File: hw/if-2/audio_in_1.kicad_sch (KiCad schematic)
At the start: 33 parts, among them U61 TL072, U62 TL072

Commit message: Documentation improvements, moved a OVP circuit
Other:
- title: COS/CTCSS/PTT Controls (Radio 1) -> Audio Input (Radio 1)
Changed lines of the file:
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@@
 	(paper "USLetter")
 	(title_block
-		(title "COS/CTCSS/PTT Controls (Radio 1)")
-		(date "2025-05-13")
+		(title "Audio Input (Radio 1)")
+		(date "2025-05-31")
 		(rev "2")
 		(company "Bruce MacKinnon KC1FSZ")

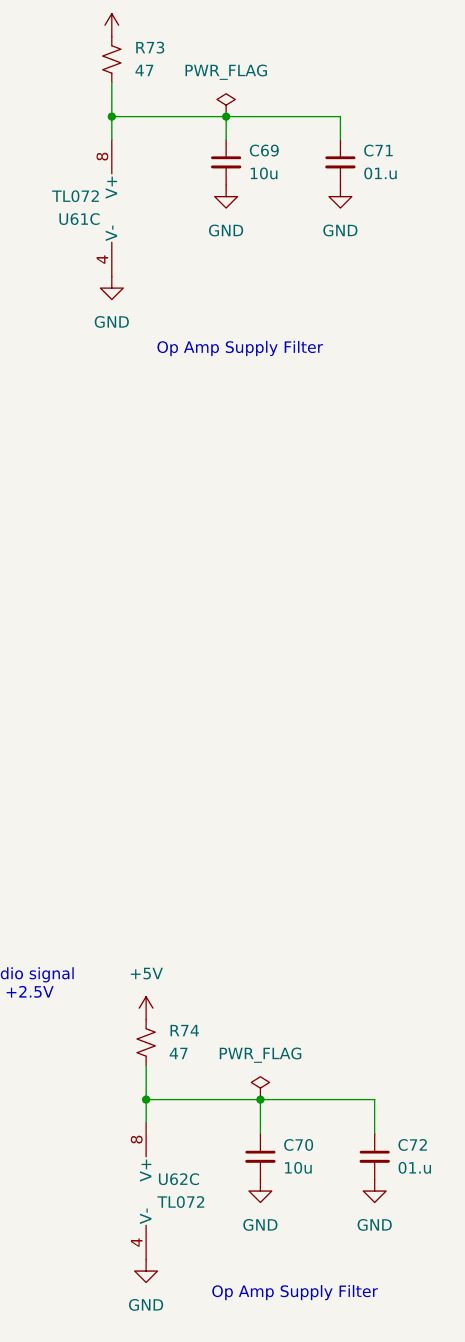
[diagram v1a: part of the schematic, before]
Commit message: Added audio clip
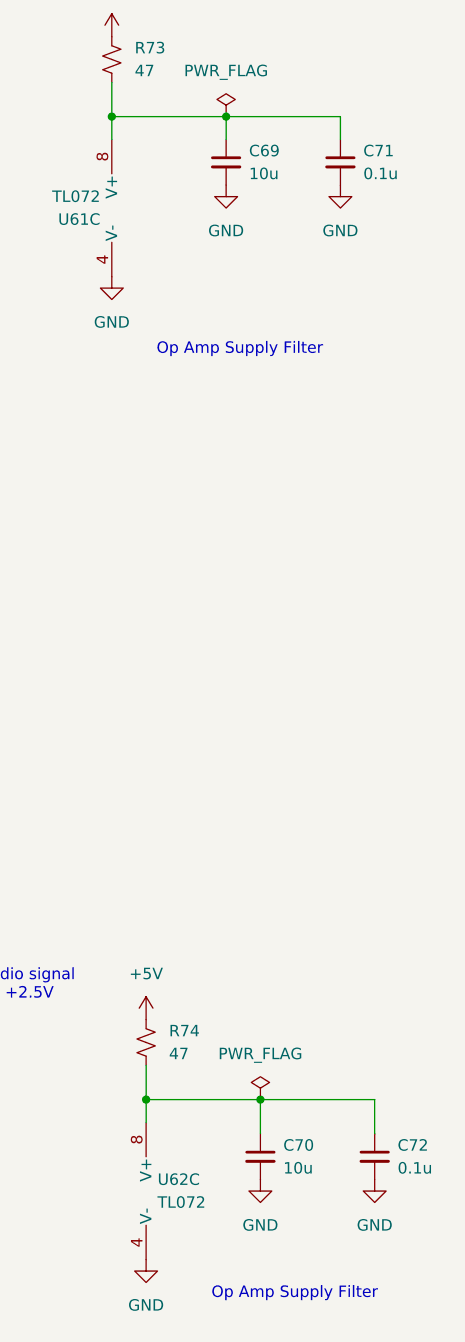
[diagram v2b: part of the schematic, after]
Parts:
- C71, C72: value 01.u -> 0.1u
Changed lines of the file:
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@@
 			)
 		)
-		(property "Value" "01.u"
+		(property "Value" "0.1u"
 			(at 248.92 36.8362 0)
 			(effects
@@
 			)
 		)
-		(property "Value" "01.u"
+		(property "Value" "0.1u"
 			(at 252.73 147.3262 0)
 			(effects

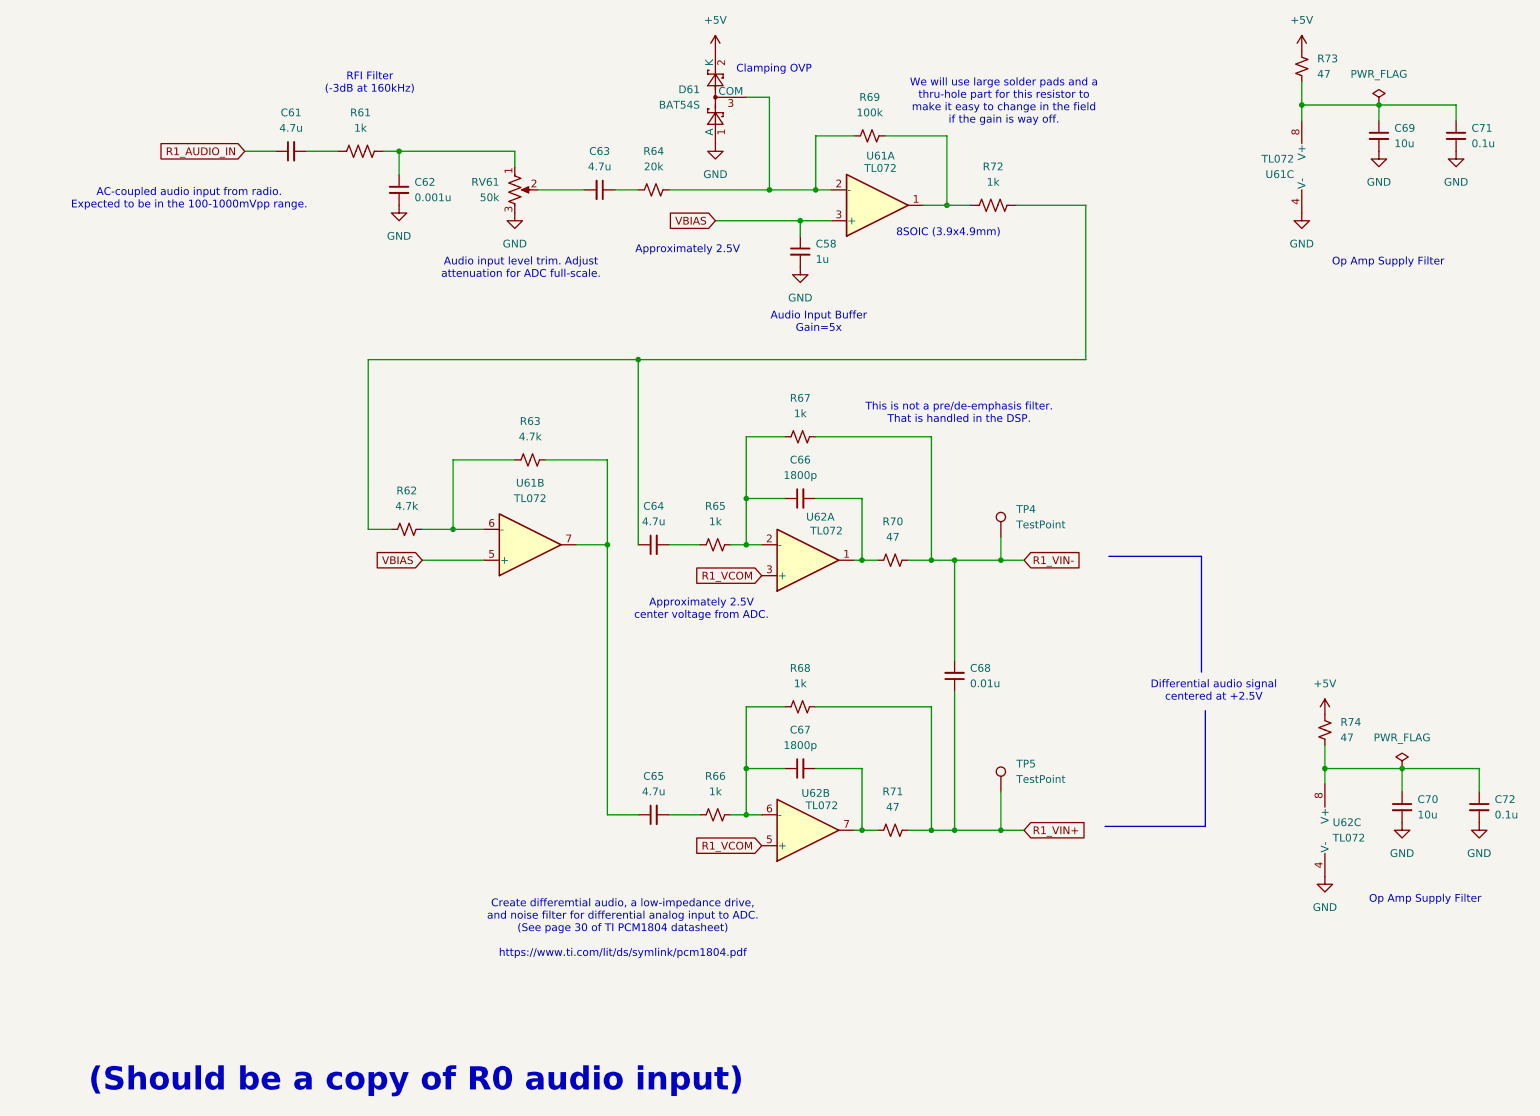
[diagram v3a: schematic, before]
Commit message: Updated audio file to 16K
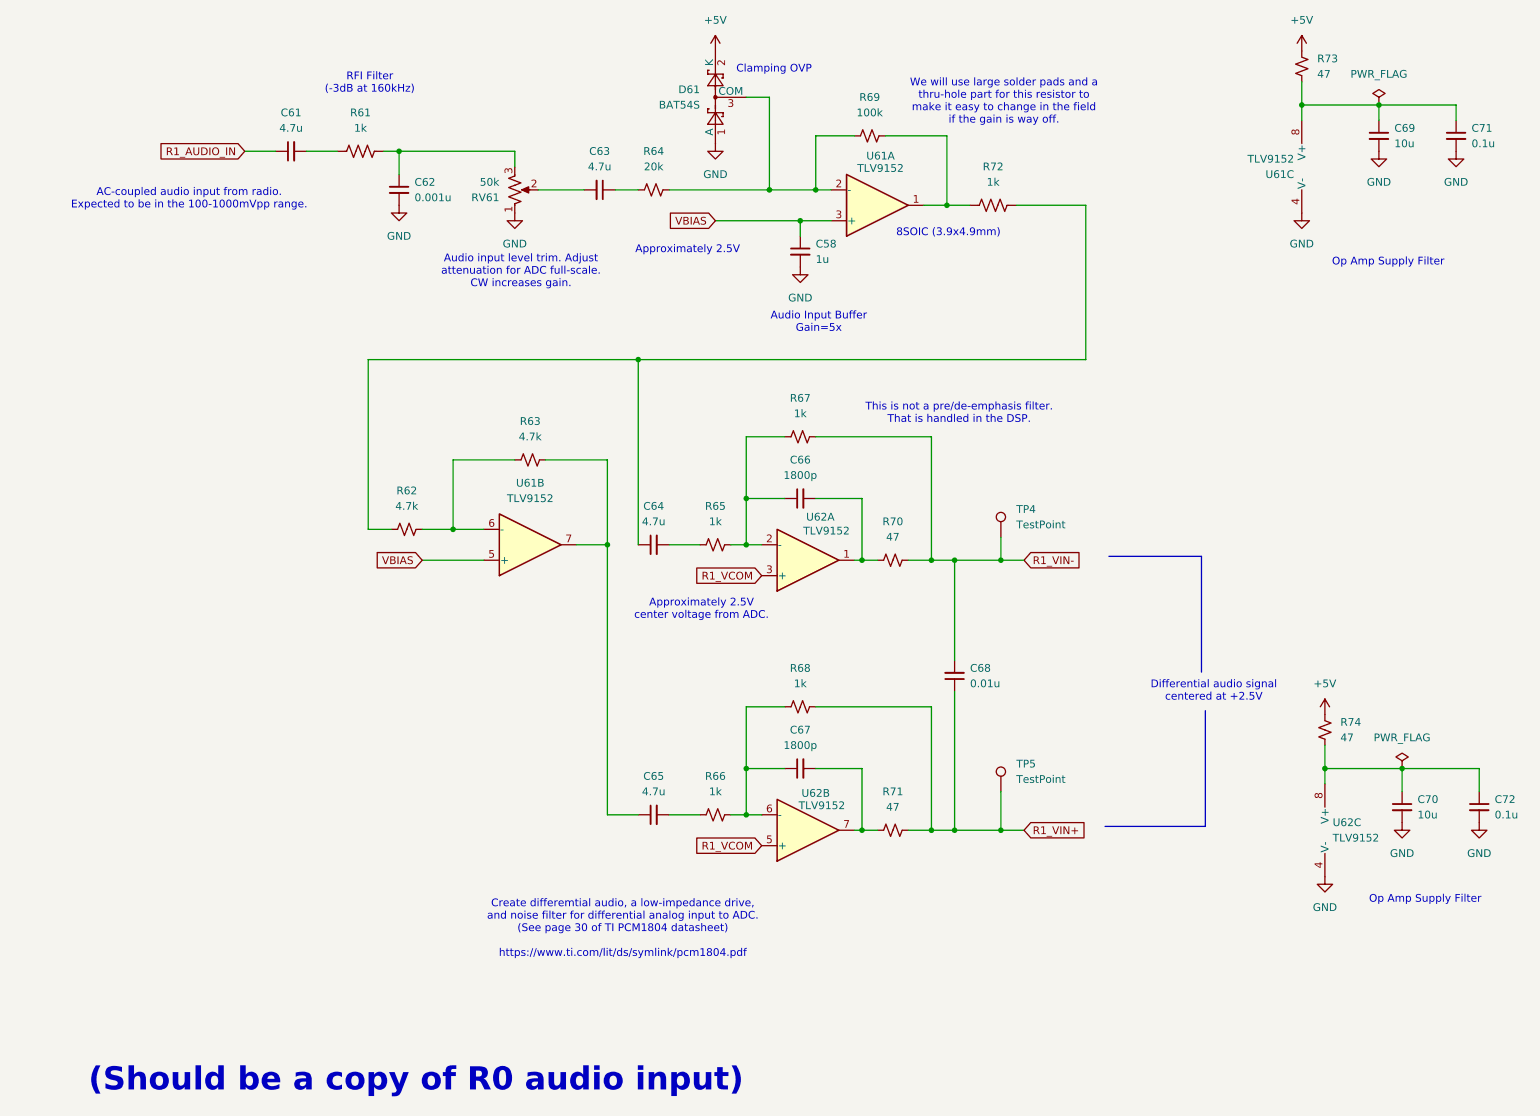
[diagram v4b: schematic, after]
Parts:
- R69: footprint Resistor_SMD:R_0805_2012Metric_Pad1.20x1.40mm_HandSolder -> Resistor_THT:R_Axial_DIN0516_L15.5mm_D5.0mm_P5.08mm_Vertical
- U61, U62: value TL072 -> TLV9152
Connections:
- net GND: now also RV61.1; no longer RV61.3
- net at C62.1, R61.2: now also RV61.3; no longer RV61.1
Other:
- note added: "Audio input level trim. Adjust attenuation for ADC full-scale. CW increases gain."
- note removed: "Audio input level trim. Adjust attenuation for ADC full-scale."
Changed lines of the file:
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@@
 		(comment 2 "NOT FOR COMMERCIAL USE")
 	)
-	(text "Audio input level trim. Adjust\nattenuation for ADC full-scale."
+	(text "Audio input level trim. Adjust\nattenuation for ADC full-scale.\nCW increases gain."
 		(exclude_from_sim no)
-		(at 92.456 57.404 0)
+		(at 92.456 57.912 0)
 		(effects
 			(font
@@
 			)
 		)
-		(property "Value" "TL072"
+		(property "Value" "TLV9152"
 			(at 93.98 95.25 0)
 			(effects
@@
 			)
 		)
-		(property "Footprint" "Resistor_SMD:R_0805_2012Metric_Pad1.20x1.40mm_HandSolder"
+		(property "Footprint" "Resistor_THT:R_Axial_DIN0516_L15.5mm_D5.0mm_P5.08mm_Vertical"
 			(at 149.86 35.56 0)
 			(effects
@@
 			)
 		)
-		(property "Value" "TL072"
+		(property "Value" "TLV9152"
 			(at 141.986 145.796 0)
 			(effects
@@
 			)
 		)
-		(property "Value" "TL072"
+		(property "Value" "TLV9152"
 			(at 142.748 100.584 0)
 			(effects
@@
 			)
 		)
-		(property "Value" "TL072"
+		(property "Value" "TLV9152"
 			(at 151.638 40.894 0)
 			(effects
@@
 			)
 		)
-		(property "Value" "TL072"
+		(property "Value" "TLV9152"
 			(at 219.71 39.3701 0)
 			(effects
@@
 		(lib_id "Device:R_Potentiometer_US")
 		(at 91.44 44.45 0)
+		(mirror x)
 		(unit 1)
 		(exclude_from_sim no)
@@
 		(on_board yes)
 		(dnp no)
-		(fields_autoplaced yes)
 		(property "Reference" "RV61"
-			(at 88.9 43.1799 0)
+			(at 88.9 45.7201 0)
 			(effects
 				(font
@@
 		)
 		(property "Value" "50k"
-			(at 88.9 45.7199 0)
+			(at 88.9 43.1801 0)
 			(effects
 				(font
@@
 			)
 		)
-		(property "Value" "TL072"
+		(property "Value" "TLV9152"
 			(at 226.06 151.1299 0)
 			(effects
